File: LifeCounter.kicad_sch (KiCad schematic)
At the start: 23 parts, among them IC1 STM32H562RGT6, IC2 AP3012KTR-E1, J1 54104-4531

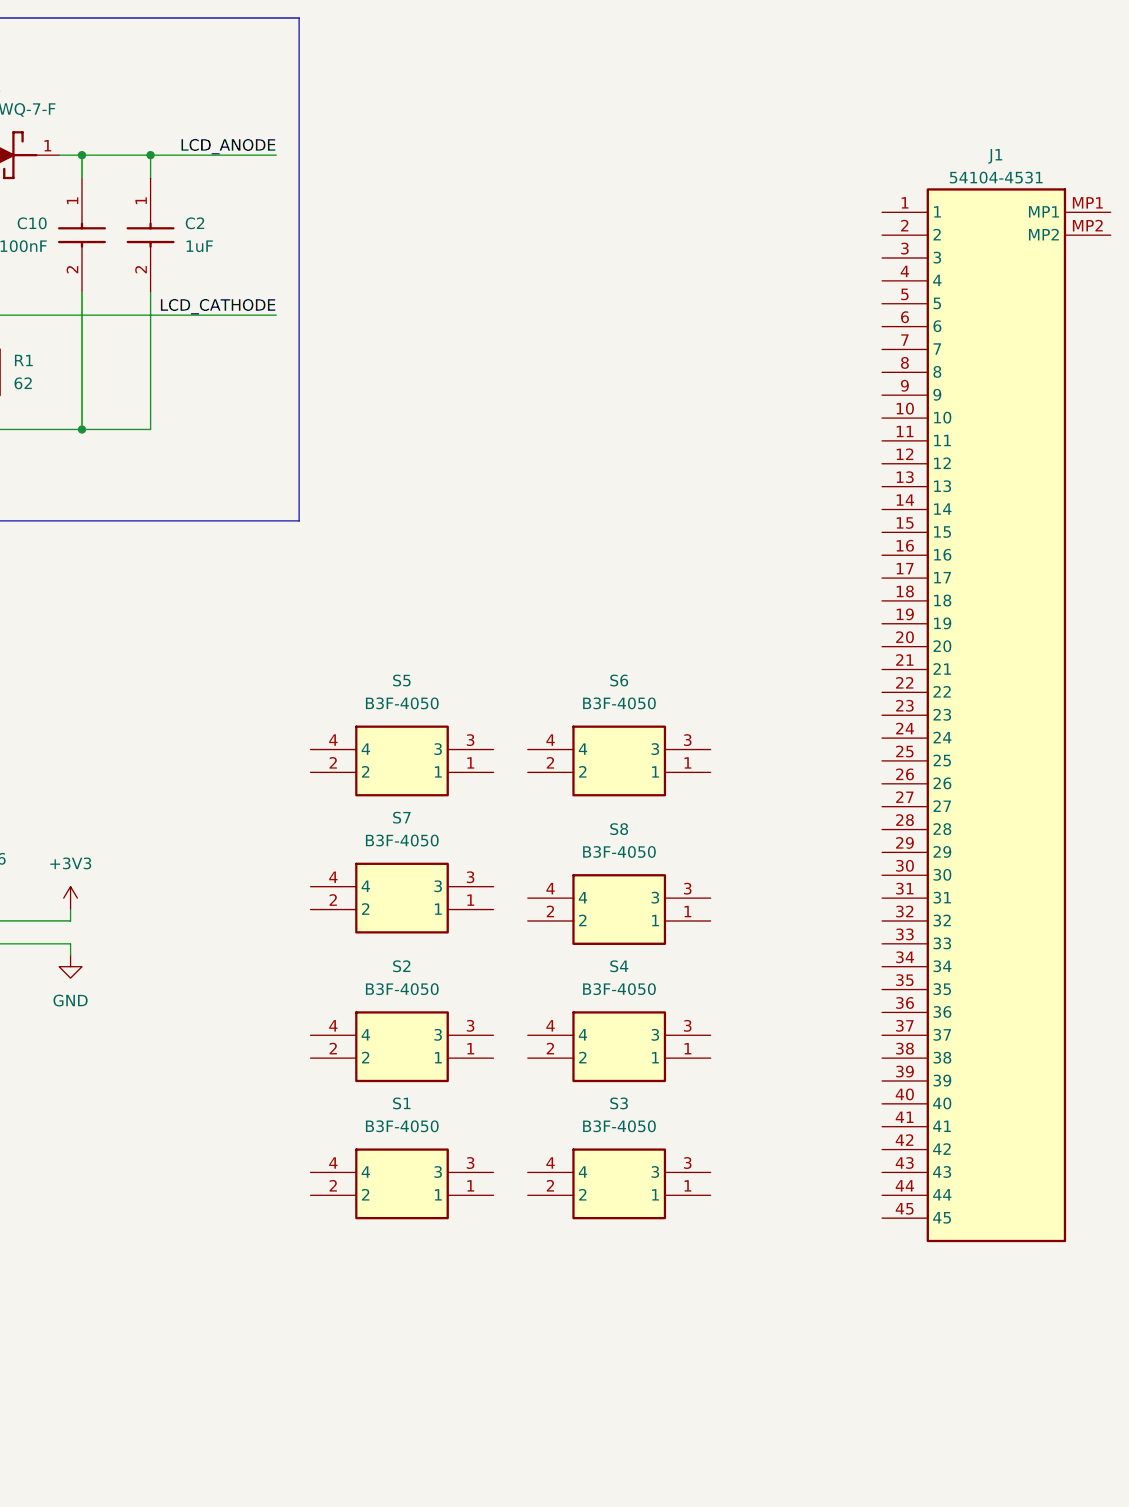
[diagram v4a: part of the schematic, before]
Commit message: labeled the FPC tape connector (LCD) pins
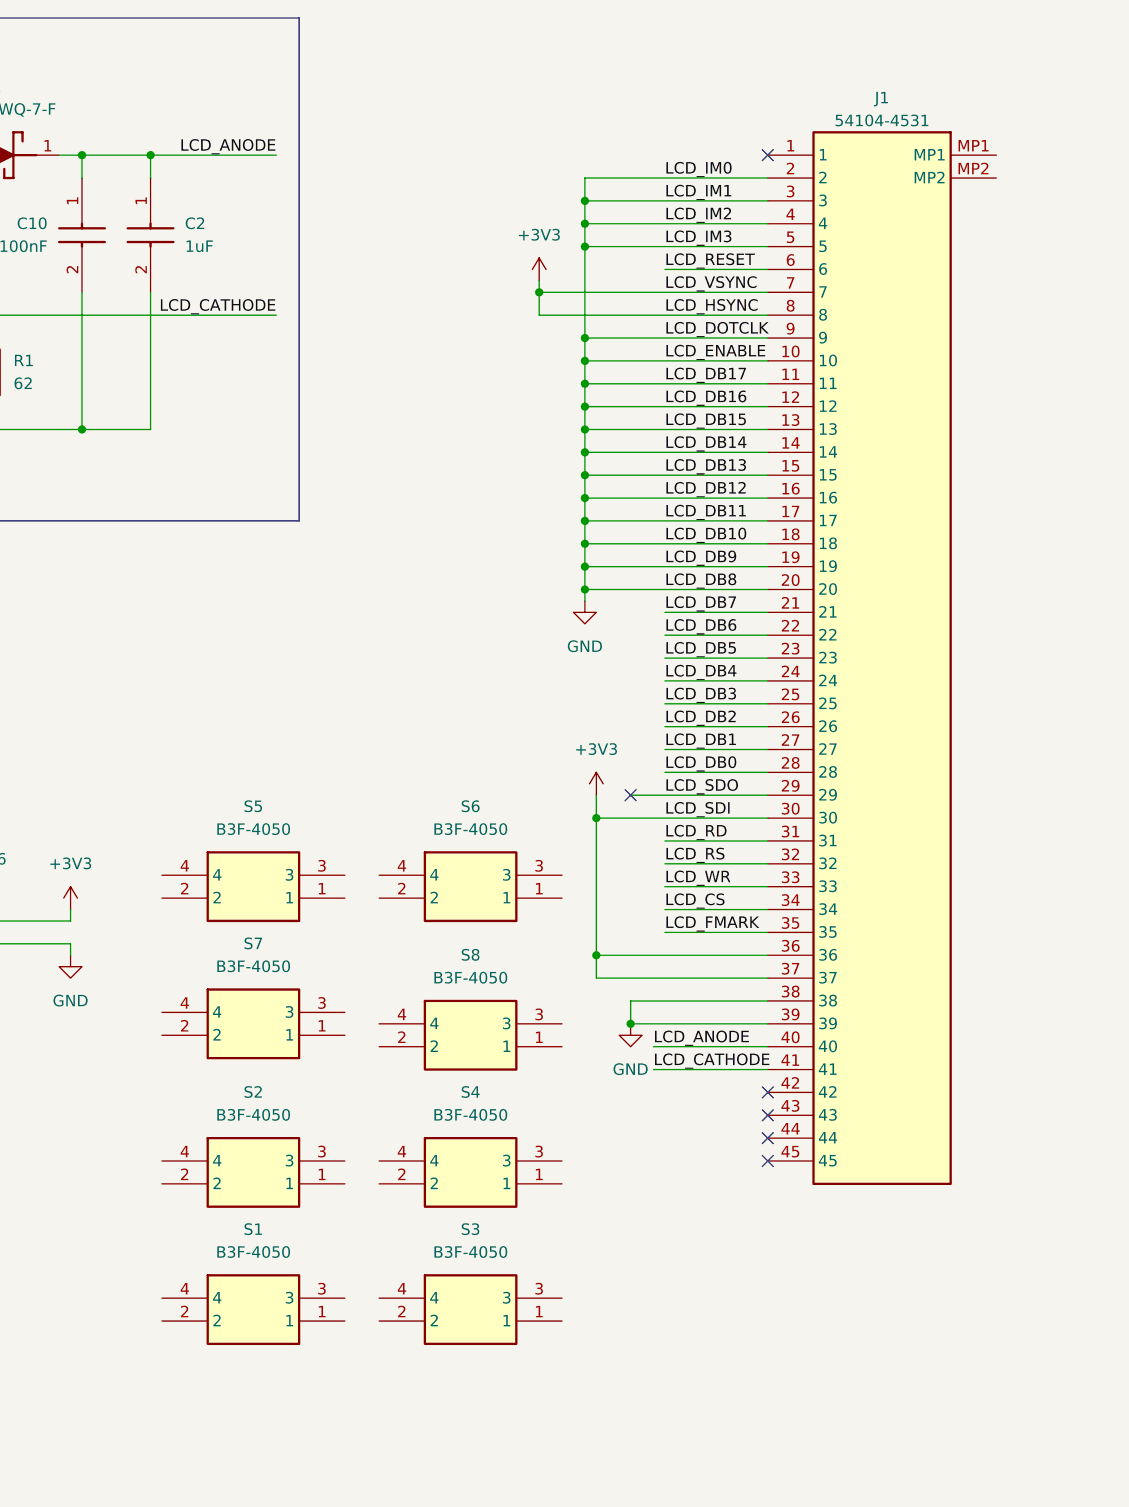
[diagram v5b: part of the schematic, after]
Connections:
- net +3V3: now also J1.30, J1.36, J1.37, J1.7, J1.8
- net GND: now also J1.10, J1.11, J1.12, J1.13, J1.14, J1.15, J1.16, J1.17, J1.18, J1.19, J1.2, J1.20, J1.3, J1.38, J1.39, J1.4, J1.5, J1.9
- net LCD_ANODE: now also J1.40
- net LCD_CATHODE: now also J1.41
- net LCD_DB7: now reaches J1.21
- net LCD_DB6: now reaches J1.22
- net LCD_DB5: now reaches J1.23
- net LCD_DB4: now reaches J1.24
- net LCD_DB3: now reaches J1.25
- net LCD_DB2: now reaches J1.26
- net LCD_DB1: now reaches J1.27
- net LCD_DB0: now reaches J1.28
- net LCD_SDO: now reaches J1.29
- net LCD_RD: now reaches J1.31
- net LCD_RS: now reaches J1.32
- net LCD_WR: now reaches J1.33
- net LCD_CS: now reaches J1.34
- net LCD_FMARK: now reaches J1.35
- net LCD_RESET: now reaches J1.6
- no-connect marks 0 -> 6
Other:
- moved on the sheet: J1, S1, S2, S3, S4, S5, S6, S7, S8

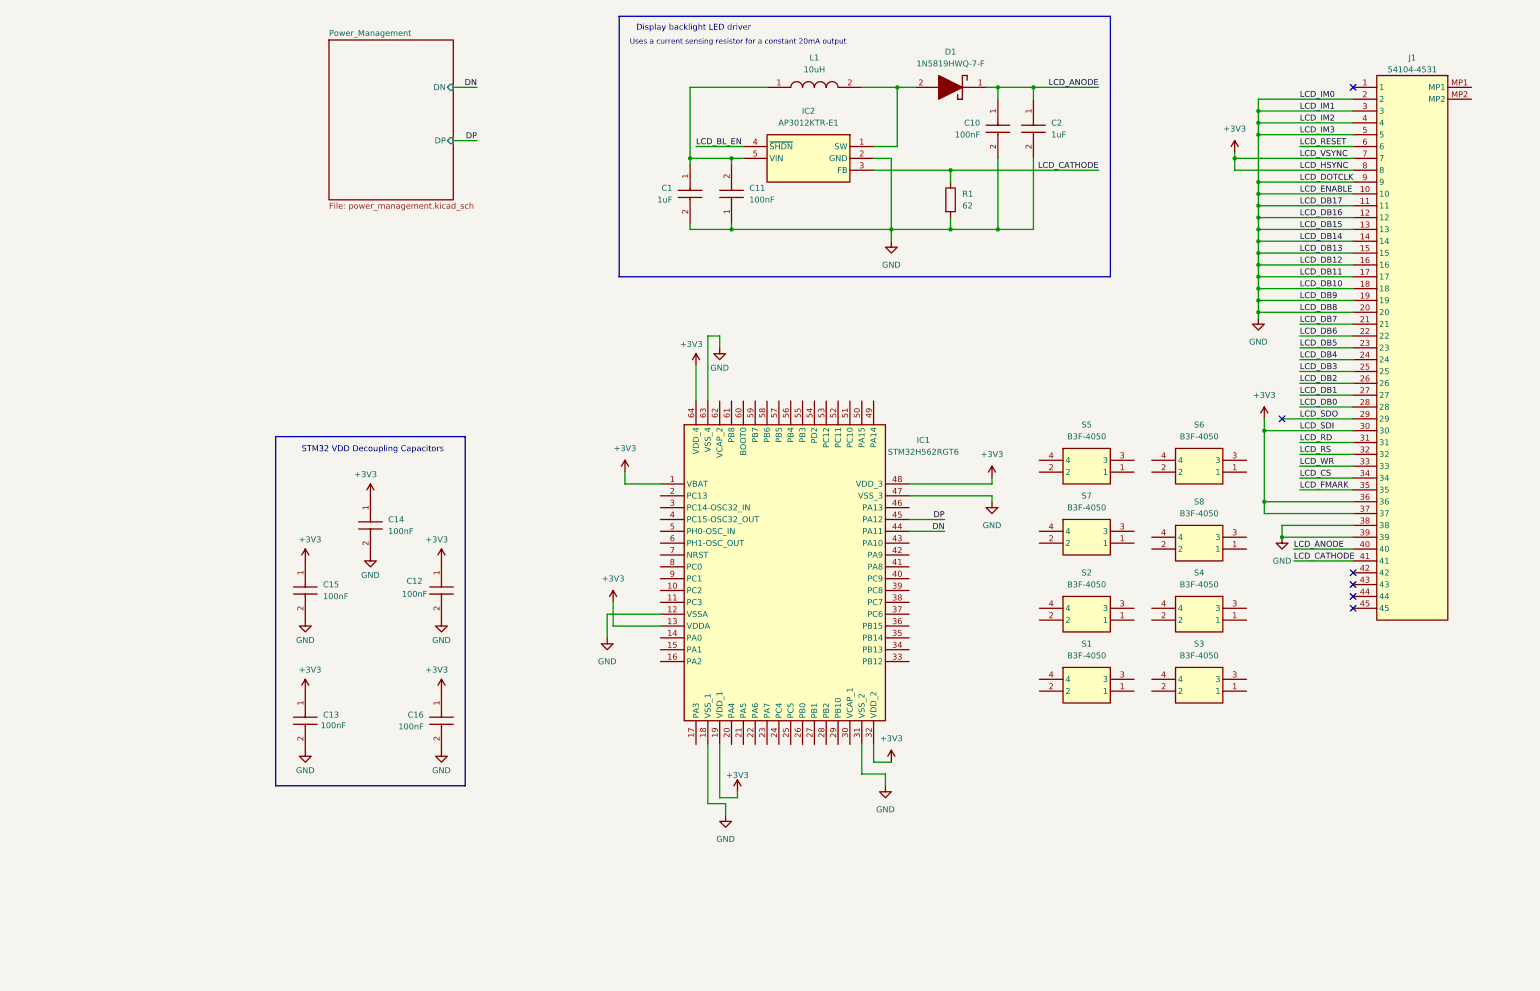
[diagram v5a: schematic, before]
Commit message: labeled the LCD pins and switched over to a 100 pin stm32 package
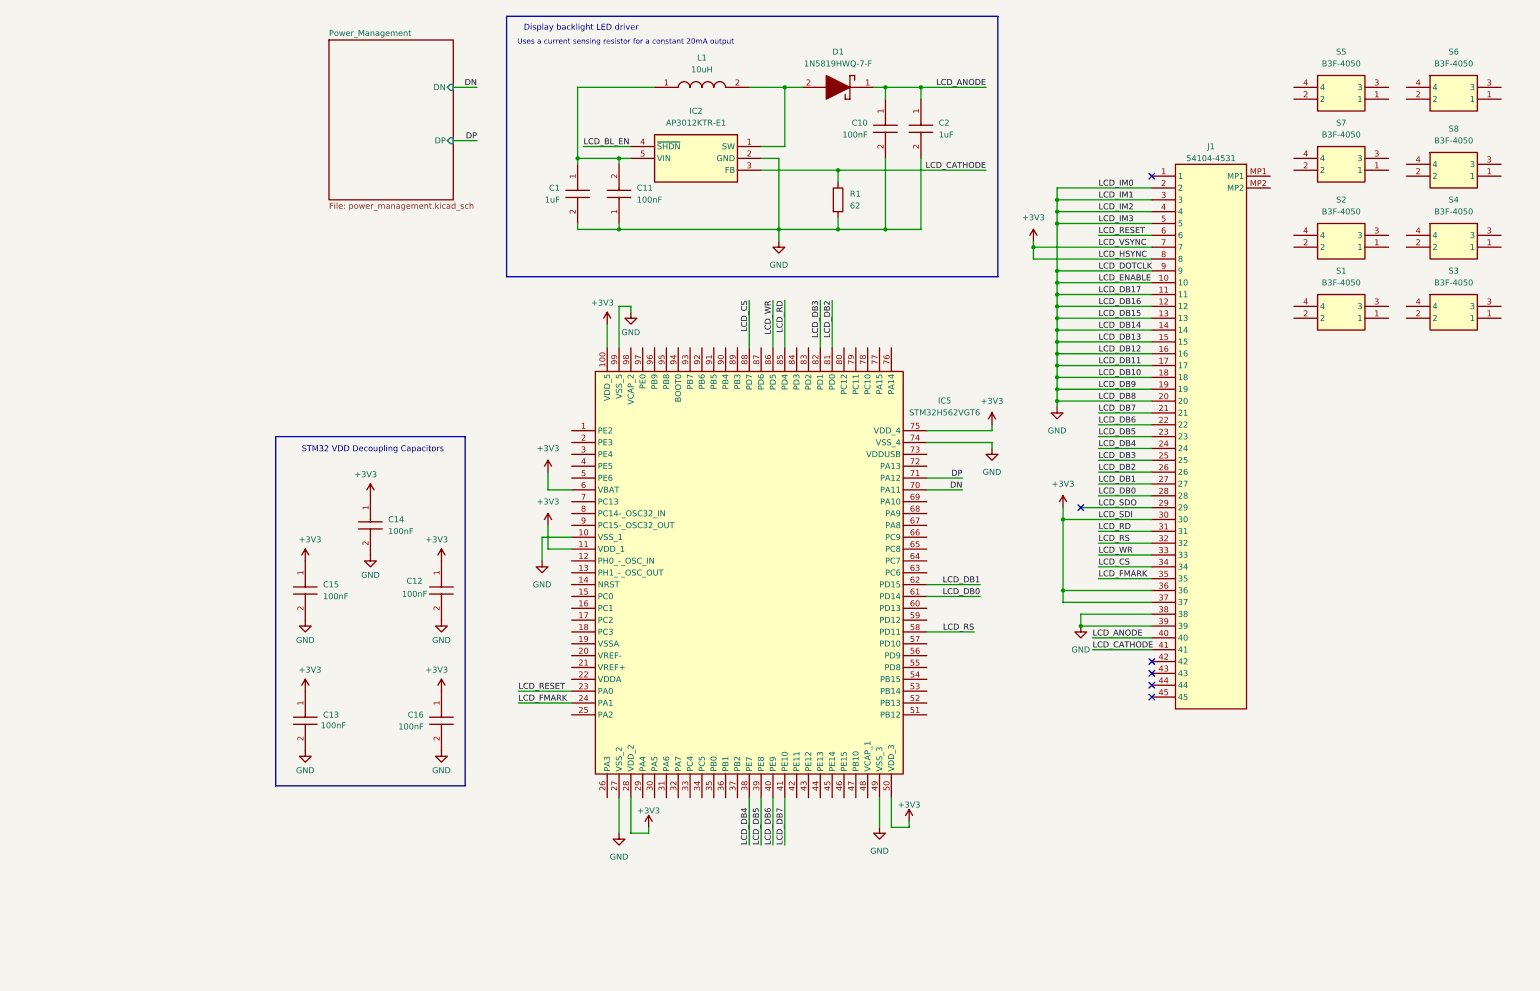
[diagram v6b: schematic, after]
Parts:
- removed IC1: STM32H562RGT6, LifeCounter-Footprints:LQFP-64_10x10mm_P0.5mm_STM32, symbol LifeCounter-Symbols:STM32H562RGT6
- added IC5: STM32H562VGT6, LifeCounter-Footprints:STMicroelectronics_QFP50P1600X1600X160-100M, symbol LifeCounter-Symbols:STM32H562VGT6
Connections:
- net +3V3: now also IC5.100 (VDD_5), IC5.11 (VDD_1), IC5.28 (VDD_2), IC5.50 (VDD_3), IC5.6 (VBAT), IC5.75 (VDD_4)
- net DN: now also IC5.70 (PA11)
- net DP: now also IC5.71 (PA12)
- net GND: now also IC5.10 (VSS_1), IC5.27 (VSS_2), IC5.49 (VSS_3), IC5.74 (VSS_4), IC5.99 (VSS_5)
- net LCD_CS: now also IC5.88 (PD7)
- net LCD_DB0: now also IC5.61 (PD14)
- net LCD_DB1: now also IC5.62 (PD15)
- net LCD_DB2: now also IC5.81 (PD0)
- net LCD_DB3: now also IC5.82 (PD1)
- net LCD_DB4: now also IC5.38 (PE7)
- net LCD_DB5: now also IC5.39 (PE8)
- net LCD_DB6: now also IC5.40 (PE9)
- net LCD_DB7: now also IC5.41 (PE10)
- net LCD_FMARK: now also IC5.24 (PA1)
- net LCD_RD: now also IC5.85 (PD4)
- net LCD_RESET: now also IC5.23 (PA0)
- net LCD_RS: now also IC5.58 (PD11)
- net LCD_WR: now also IC5.86 (PD5)
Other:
- moved on the sheet: C1, C10, C11, C2, D1, IC2, J1, L1, R1, S1, S2, S3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
